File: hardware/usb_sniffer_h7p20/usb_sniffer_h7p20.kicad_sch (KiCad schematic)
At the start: 93 parts, among them J1 FPGA_JTAG, J4 USB_C_Receptacle_USB2.0_16P, J5 FFC-40P-0.5mm,NC, J6 Trigger, U1 H7P20N0L128-M3H1, U6 ZB25VQ16CTJG, U7 CY7C68013A-56LTX, U8 24C32, U9 CJ3439KDW, Y2 24M

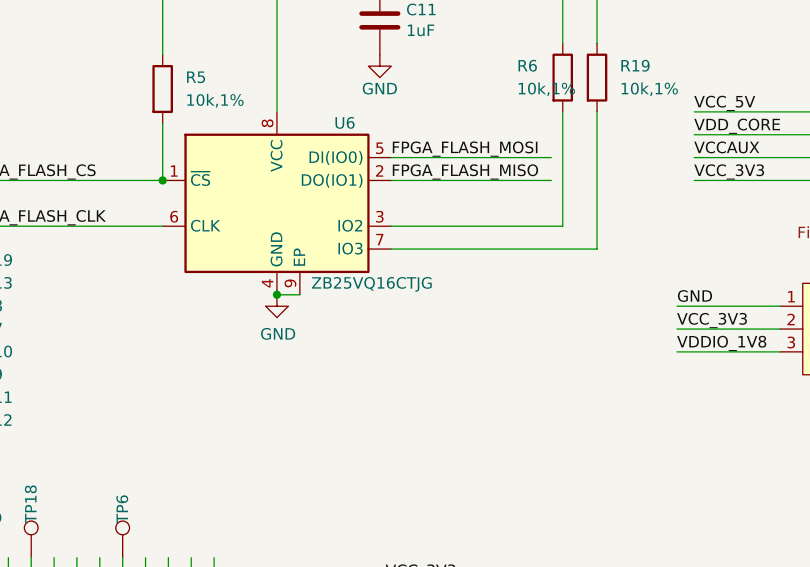
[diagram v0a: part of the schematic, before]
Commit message: [usb_sniffer_h7p20] 统一使用P25Q64SH-SSH-IR
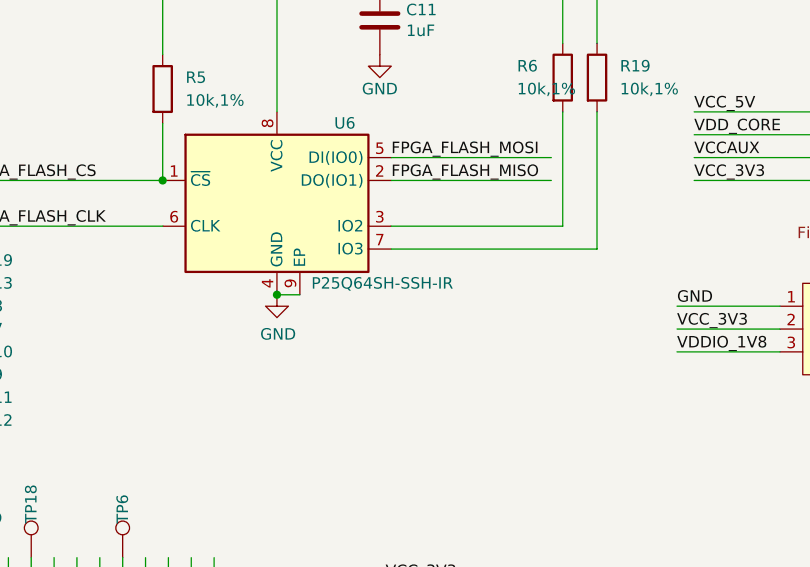
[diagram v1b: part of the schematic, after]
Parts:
- U6: value ZB25VQ16CTJG -> P25Q64SH-SSH-IR
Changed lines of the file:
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@@
 			)
 		)
-		(property "Value" "ZB25VQ16CTJG"
+		(property "Value" "P25Q64SH-SSH-IR"
 			(at 240.665 49.53 0)
 			(effects

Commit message: [usb_sniffer_h7p20] production_files.20250828
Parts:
- R12: value 5.1k,1% -> 10k,1%
- R8: value 10k,1% -> 4.7k,1%
- R9: value 5.1k,1% -> 4.7k,1%
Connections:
- net VCC_5V: now also J5.1 (Pin_1)
- no-connect marks 6 -> 5
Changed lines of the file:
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@@
 	)
 	(no_connect
-		(at 243.84 246.38)
-	)
-	(no_connect
 		(at 238.76 246.38)
 	)
@@
 		)
 	)
+	(label "VCC_5V"
+		(at 243.84 246.38 90)
+		(effects
+			(font
+				(size 1.27 1.27)
+			)
+			(justify left bottom)
+		)
+	)
 	(label "VDD_CORE"
 		(at 281.94 189.23 0)
@@
 			)
 		)
-		(property "Value" "5.1k,1%"
+		(property "Value" "4.7k,1%"
 			(at 132.08 59.69 90)
 			(effects
@@
 			)
 		)
-		(property "Value" "10k,1%"
+		(property "Value" "4.7k,1%"
 			(at 132.08 49.53 90)
 			(effects
@@
 			)
 		)
-		(property "Value" "5.1k,1%"
+		(property "Value" "10k,1%"
 			(at 132.08 54.61 90)
 			(effects
